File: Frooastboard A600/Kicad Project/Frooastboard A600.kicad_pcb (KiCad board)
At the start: 2 copper layers, 319.1 x 128.6 mm, 207 parts, among them J1 PS2_5V, J3 SW Interface, J8 USB, Q1 BSS138, Q2 BSS138, U2 RP2040, U3 W25Q32JVZP, U4 LM317L_SOT-89, Y1 12MHz

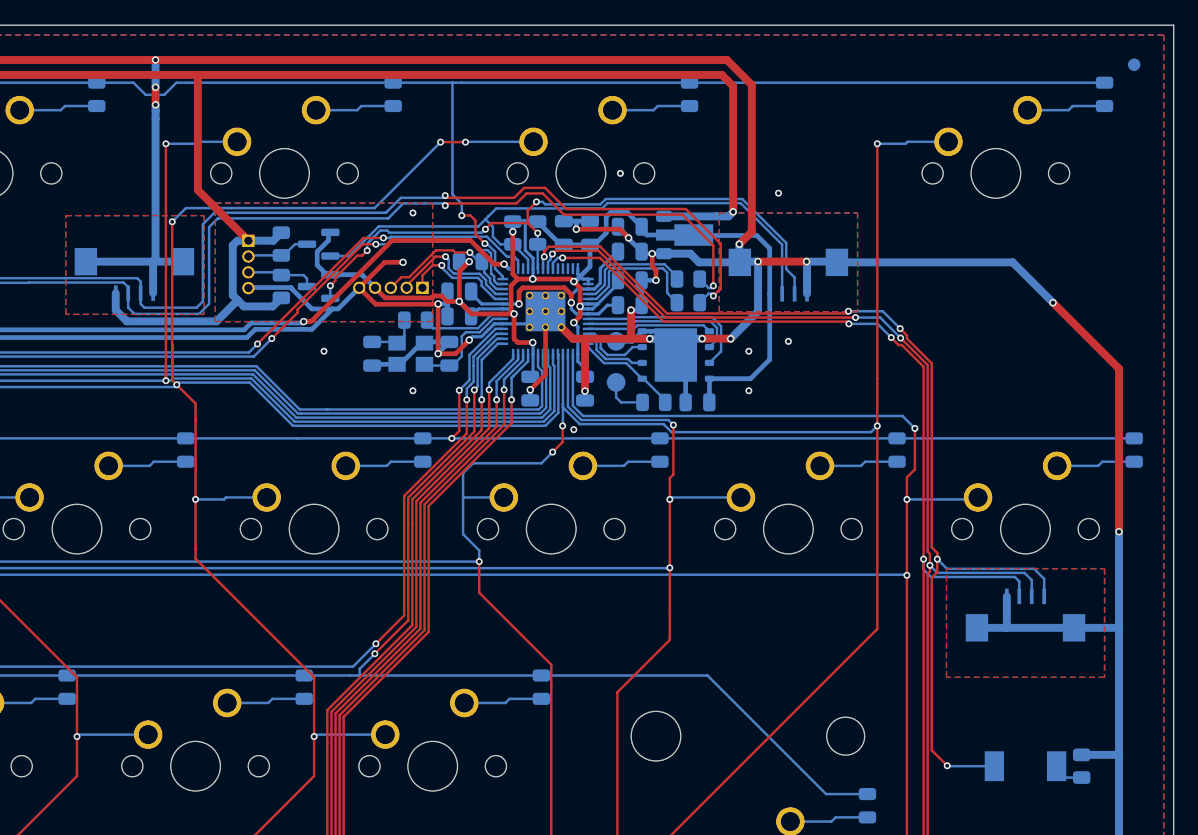
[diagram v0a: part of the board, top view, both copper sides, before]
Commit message: fix 4pin (other still wrong)
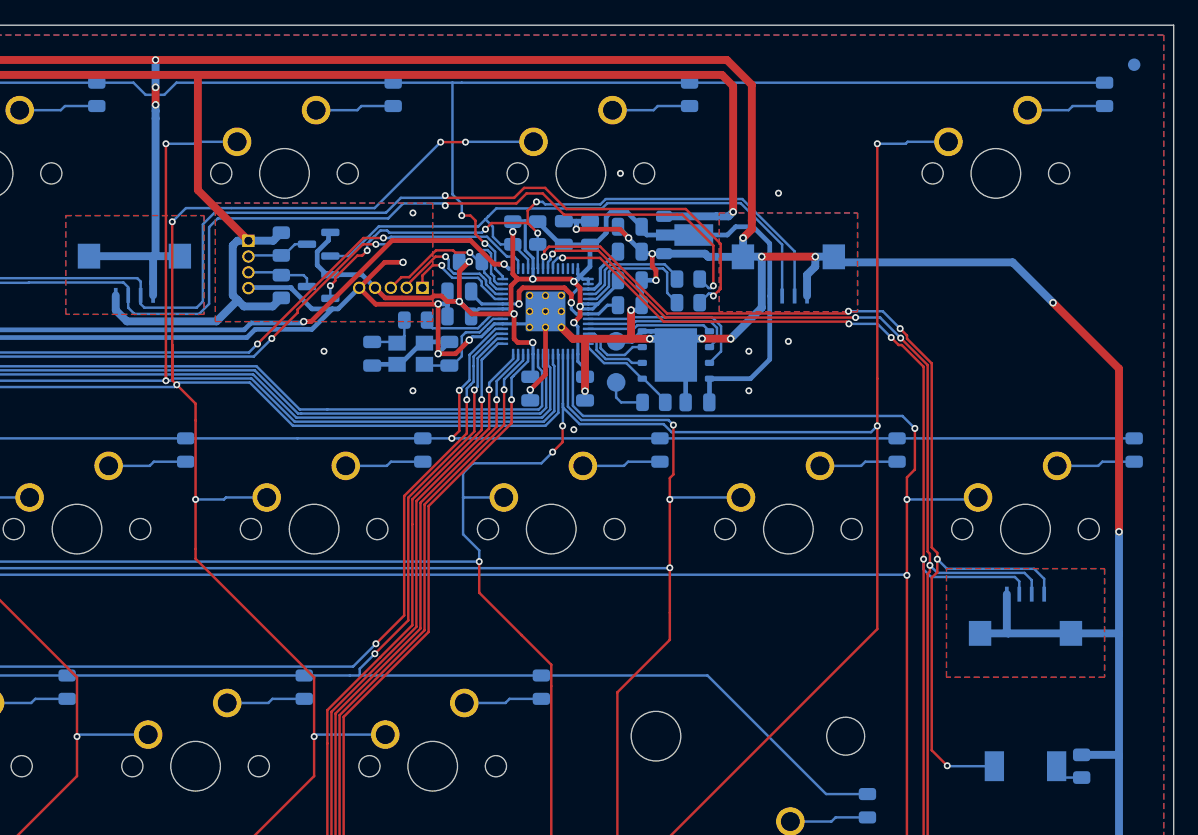
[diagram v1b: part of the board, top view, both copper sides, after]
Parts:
- removed FPC3: AFA01-S04FCC-00, AFA01-SXXFCX-00:FPC-SMD_4P-P1.00_AFA01-S04FCC-00
- added FPC4: AFA24-S04FIA-HF, AFA24-SXXFIA-HF:FPC-SMD_4P-P1.00_AFA24-S04FIA-HF, B.Cu at (260.2, 33.6)
- FPC1, FPC2: value AFA01-S04FCC-00 -> AFA24-S04FIA-HF; footprint AFA01-SXXFCX-00:FPC-SMD_4P-P1.00_AFA01-S04FCC-00 -> AFA24-SXXFIA-HF:FPC-SMD_4P-P1.00_AFA24-S04FIA-HF
- moved FPC2 52.5 mm to (312.7, 33.7)
- moved FPC1 30.7 mm to (331.8, 57.6), turned to 180 degrees
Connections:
- FPC1 pad 1: +3.3V -> Net-(D26-A)
- FPC1 pad 2: PS2_Clock -> Net-(D16-A)
- FPC1 pad 3: PS2_Data -> Net-(D6-A)
- FPC2 pad 1: +5V -> +3.3V
- FPC2 pad 2: RP_D- -> PS2_Clock
- FPC2 pad 3: RP_D+ -> PS2_Data
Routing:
- net +3.3V: track 115.4 -> 116.3 mm
- net GND: track 770.5 -> 771.0 mm

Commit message: make more space on the edges
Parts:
- moved D54 22.4 mm to (315.9, 19.8), turned to 90 degrees
- moved D107 10.3 mm to (330.2, 46.0)
- moved D72 10.3 mm to (330.2, 122.2)
- moved FID2 9.00 mm to (333.8, 21.0)
- moved J8 8.61 mm to (182.6, 27.6)
- moved FID1 5.61 mm to (32.5, 132.6)
- moved D1 2.38 mm to (47.6, 19.8), turned to 90 degrees
- moved D11 2.38 mm to (81.0, 19.8), turned to 90 degrees
- moved D17 2.38 mm to (233.4, 19.8), turned to 90 degrees
- moved D21 2.38 mm to (104.8, 19.8), turned to 90 degrees
- moved D27 2.38 mm to (257.2, 19.8), turned to 90 degrees
- moved D31 2.38 mm to (128.6, 19.8), turned to 90 degrees
- moved D36 2.38 mm to (281.0, 19.8), turned to 90 degrees
- moved D40 2.38 mm to (152.4, 19.8), turned to 90 degrees
- moved D45 2.38 mm to (304.8, 19.8), turned to 90 degrees
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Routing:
- net col0: track 585.4 -> 545.1 mm, vias 13 -> 6
- net row0: track 301.7 -> 269.5 mm
- net GND: track 771.0 -> 742.1 mm, vias 36 -> 47
- net row1: track 147.3 -> 128.5 mm
- net row10: track 372.2 -> 361.9 mm
- net row3: track 144.2 -> 133.9 mm
- net Net-(D54-A): track 6.33 -> 16.4 mm
- net +5V: track 209.2 -> 200.4 mm, vias 6 -> 4
- net RP_D-: track 162.1 -> 158.2 mm, vias 4 -> 2
- net RP_D+: track 162.8 -> 158.9 mm, vias 4 -> 2
- net Net-(D72-A): track 6.33 -> 4.27 mm
- net Net-(D107-A): track 6.33 -> 4.27 mm
